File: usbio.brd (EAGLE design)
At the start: 12.3 x 40.1 mm, 19 parts, among them U1 ATMEGA328P-MU-QFN32

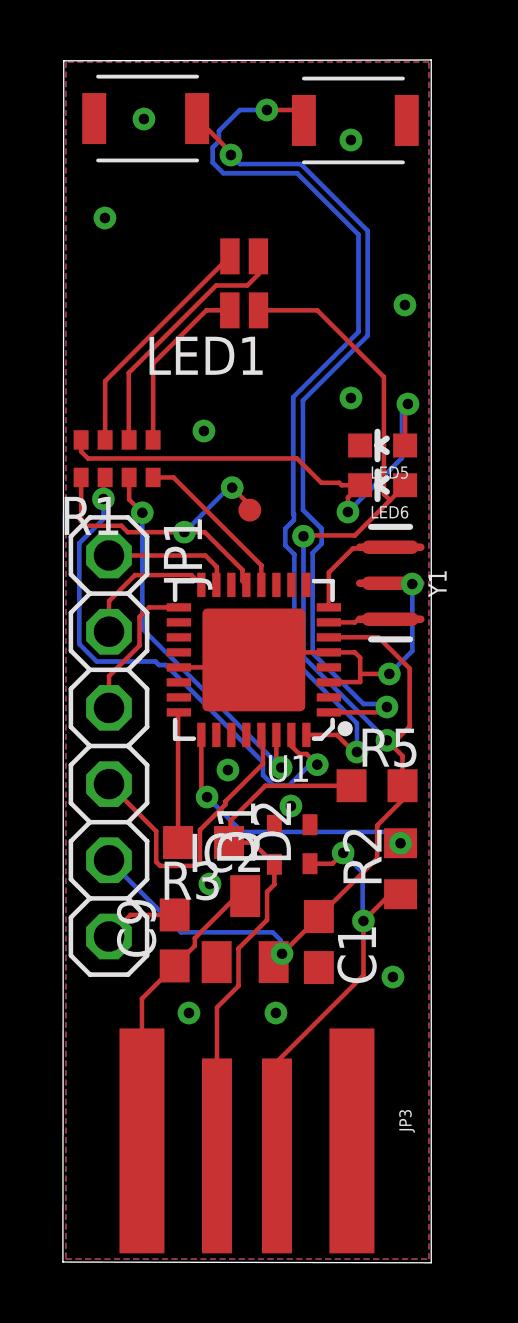
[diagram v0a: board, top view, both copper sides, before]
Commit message: Correct routing to led
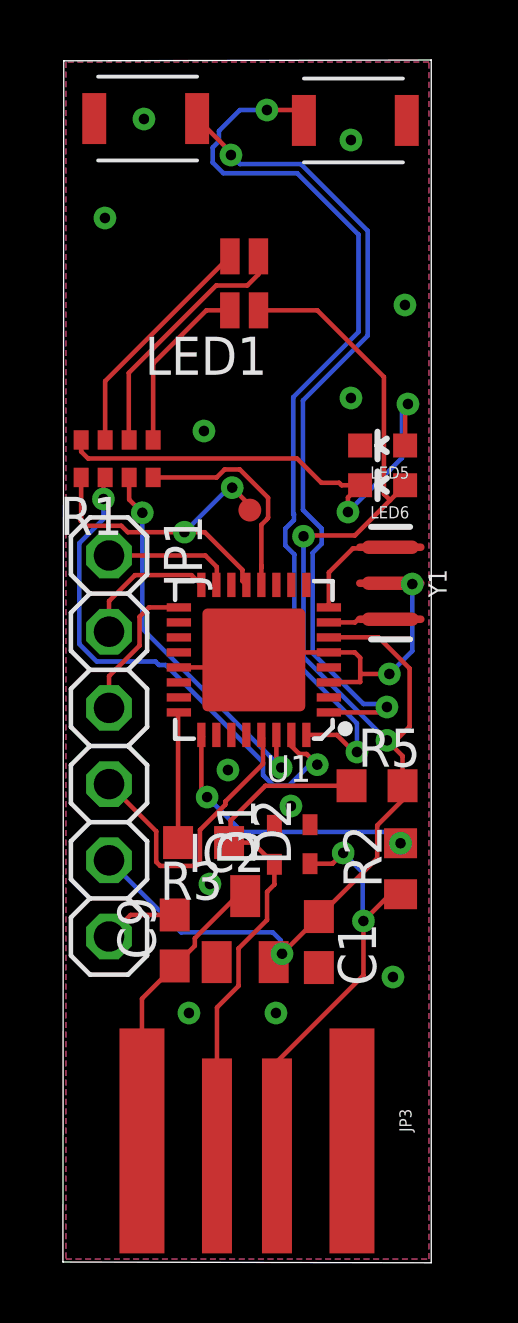
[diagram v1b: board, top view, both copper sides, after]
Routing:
- net LED: track 5.47 -> 7.33 mm
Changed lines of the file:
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@@
 <contactref element="R1" pad="4"/>
 <contactref element="U1" pad="12"/>
-<wire x1="3.007" y1="26.152" x2="3.683" y2="26.152" width="0.1524" layer="1"/>
-<wire x1="3.683" y1="26.152" x2="6.615" y2="23.22" width="0.1524" layer="1"/>
-<wire x1="6.615" y1="23.22" x2="6.614" y2="23.219" width="0.1524" layer="1"/>
-<wire x1="6.614" y1="23.219" x2="6.614" y2="22.57" width="0.1524" layer="1"/>
+<wire x1="6.614" y1="23.219" x2="6.614" y2="23.1394" width="0.1524" layer="1"/>
+<wire x1="6.614" y1="23.1394" x2="6.614" y2="22.57" width="0.1524" layer="1"/>
+<wire x1="3.007" y1="26.152" x2="5.12485" y2="26.152" width="0.1524" layer="1"/>
+<wire x1="5.12485" y1="26.152" x2="5.39165" y2="26.4188" width="0.1524" layer="1"/>
+<wire x1="5.39165" y1="26.4188" x2="5.89435" y2="26.4188" width="0.1524" layer="1"/>
+<wire x1="6.8396" y1="24.81149375" x2="6.8072" y2="24.77909375" width="0.1524" layer="1"/>
+<wire x1="6.8072" y1="24.77909375" x2="6.8072" y2="24.765" width="0.1524" layer="1"/>
+<wire x1="5.89435" y1="26.4188" x2="6.8396" y2="25.47355" width="0.1524" layer="1"/>
+<wire x1="6.8396" y1="25.47355" x2="6.8396" y2="24.81149375" width="0.1524" layer="1"/>
+<wire x1="6.8072" y1="24.765" x2="6.614" y2="24.5718" width="0.1524" layer="1"/>
+<wire x1="6.614" y1="24.5718" x2="6.614" y2="23.219" width="0.1524" layer="1"/>
 </signal>
 <signal name="+3V3">

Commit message: Route missing signals, fix warnings
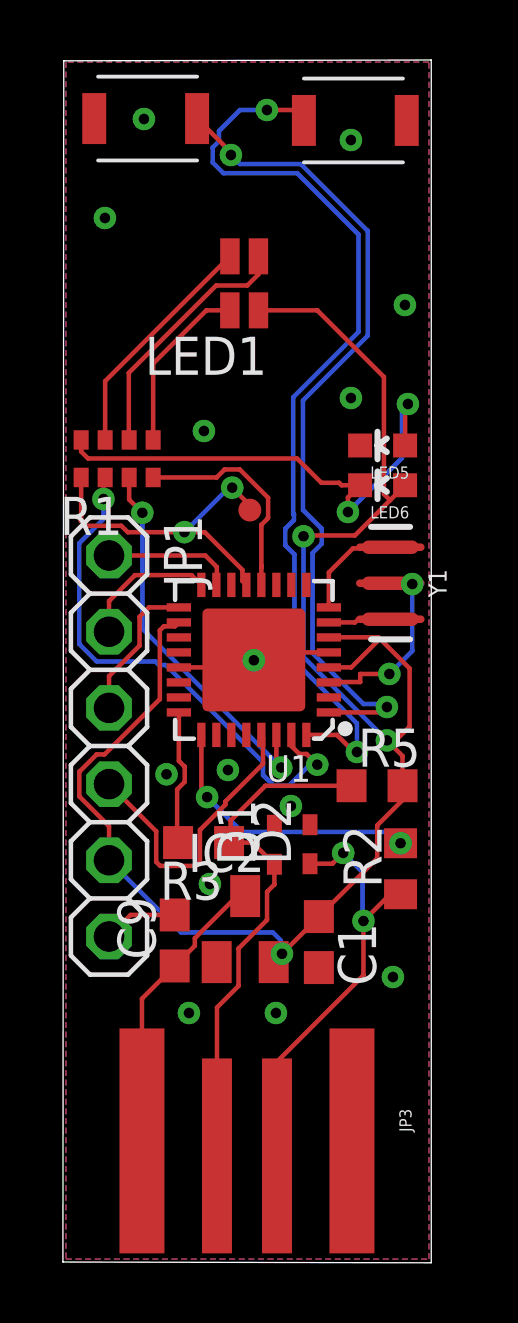
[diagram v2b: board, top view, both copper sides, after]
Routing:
- net +3V3: track 44.3 -> 56.5 mm
- net GND: track 15.7 -> 14.0 mm, vias 14 -> 16
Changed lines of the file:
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@@
 <contactref element="IC2" pad="1"/>
 <contactref element="C9" pad="2"/>
-<wire x1="8.864" y1="20.32" x2="9.731" y2="20.32" width="0.1524" layer="1"/>
-<wire x1="9.731" y1="20.32" x2="9.909" y2="20.142" width="0.1524" layer="1"/>
-<wire x1="9.909" y1="20.142" x2="9.909" y2="19.602" width="0.1524" layer="1"/>
 <wire x1="9.909" y1="19.602" x2="9.909" y2="19.332" width="0.1524" layer="1"/>
 <wire x1="9.909" y1="19.332" x2="8.876" y2="19.332" width="0.1524" layer="1"/>
@@
 <via x="7.6" y="15.2" extent="1-16" drill="0.35"/>
 <via x="5.5" y="16.4" extent="1-16" drill="0.35"/>
+<via x="6.3636" y="20.0576" extent="1-16" drill="0.35"/>
+<via x="3.4522" y="16.2576" extent="1-16" drill="0.35"/>
 </signal>
 <signal name="LED">
@@
 <wire x1="10.51785" y1="20.8233" x2="8.8673" y2="20.8233" width="0.1524" layer="1"/>
 <wire x1="8.864" y1="20.82" x2="8.8673" y2="20.8233" width="0.1524" layer="1"/>
-<wire x1="10.51785" y1="20.8233" x2="11.556" y2="19.78515" width="0.1524" layer="1"/>
+<wire x1="10.51785" y1="20.8233" x2="10.565175" y2="20.775975" width="0.1524" layer="1"/>
+<wire x1="10.565175" y1="20.775975" x2="11.556" y2="19.78515" width="0.1524" layer="1"/>
 <wire x1="11.556" y1="19.78515" x2="11.556" y2="17.847" width="0.1524" layer="1"/>
 <wire x1="11.556" y1="17.847" x2="11.0295" y2="17.3205" width="0.1524" layer="1"/>
@@
 <wire x1="10.7" y1="29.5" x2="10.7" y2="25.6" width="0.1524" layer="1"/>
 <wire x1="10.7" y1="25.6" x2="10.907" y2="25.393" width="0.1524" layer="1"/>
-<wire x1="8.019" y1="20.169" x2="8.864" y2="19.82" width="0" layer="19" extent="1-16"/>
-<wire x1="3.864" y1="21.32" x2="8.019" y2="20.169" width="0" layer="19" extent="1-16"/>
+<wire x1="3.864" y1="21.32" x2="3.7323" y2="21.1883" width="0.1524" layer="1"/>
+<wire x1="3.7323" y1="21.1883" x2="3.3629125" y2="21.1883" width="0.1524" layer="1"/>
+<wire x1="3.3629125" y1="21.1883" x2="3.229" y2="21.0543875" width="0.1524" layer="1"/>
+<wire x1="1.125675" y1="16.9206" x2="0.5454" y2="16.340325" width="0.1524" layer="1"/>
+<wire x1="0.5454" y1="16.340325" x2="0.5454" y2="15.519675" width="0.1524" layer="1"/>
+<wire x1="1.387525" y1="16.9206" x2="1.125675" y2="16.9206" width="0.1524" layer="1"/>
+<wire x1="1.536" y1="14.529075" x2="1.536" y2="13.39" width="0.1524" layer="1"/>
+<wire x1="0.5454" y1="15.519675" x2="1.536" y2="14.529075" width="0.1524" layer="1"/>
+<wire x1="3.229" y1="21.0543875" x2="3.229" y2="18.762075" width="0.1524" layer="1"/>
+<wire x1="3.229" y1="18.762075" x2="1.387525" y2="16.9206" width="0.1524" layer="1"/>
+<wire x1="8.864" y1="19.82" x2="9.6092" y2="19.82" width="0.1524" layer="1"/>
+<wire x1="9.6092" y1="19.82" x2="10.565175" y2="20.775975" width="0.1524" layer="1"/>
 </signal>
 <signal name="ADCENA">
@@
 <contactref element="U1" pad="24"/>
 <wire x1="3.838" y1="13.981" x2="3.459" y2="14.36" width="0.1524" layer="1"/>
-<wire x1="3.838" y1="13.981" x2="3.838" y2="18.294" width="0.1524" layer="1"/>
 <wire x1="3.838" y1="18.294" x2="3.864" y2="18.32" width="0.1524" layer="1"/>
+<wire x1="3.864" y1="18.32" x2="3.864" y2="16.70395" width="0.1524" layer="1"/>
+<wire x1="3.864" y1="16.70395" x2="4.059" y2="16.50895" width="0.1524" layer="1"/>
+<wire x1="4.059" y1="16.50895" x2="4.059" y2="16.00625" width="0.1524" layer="1"/>
+<wire x1="4.059" y1="16.00625" x2="3.805375" y2="15.752625" width="0.1524" layer="1"/>
+<wire x1="3.805375" y1="15.752625" x2="3.805375" y2="14.013625" width="0.1524" layer="1"/>
+<wire x1="3.805375" y1="14.013625" x2="3.838" y2="13.981" width="0.1524" layer="1"/>
 </signal>
 <signal name="D+">
@@
 <mfgpreviewcolor name="substratecolor" color="0xFF786E46"/>
 </mfgpreviewcolors>
+<errors>
+</errors>
 </board>
 </drawing>
